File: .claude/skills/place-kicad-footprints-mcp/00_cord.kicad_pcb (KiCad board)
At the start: 2 copper layers, 38.7 x 20 mm, 7 parts, among them J1 Conn_01x02, J2 Conn_01x02, J3 Conn_01x02, U1 TPS62204DBV

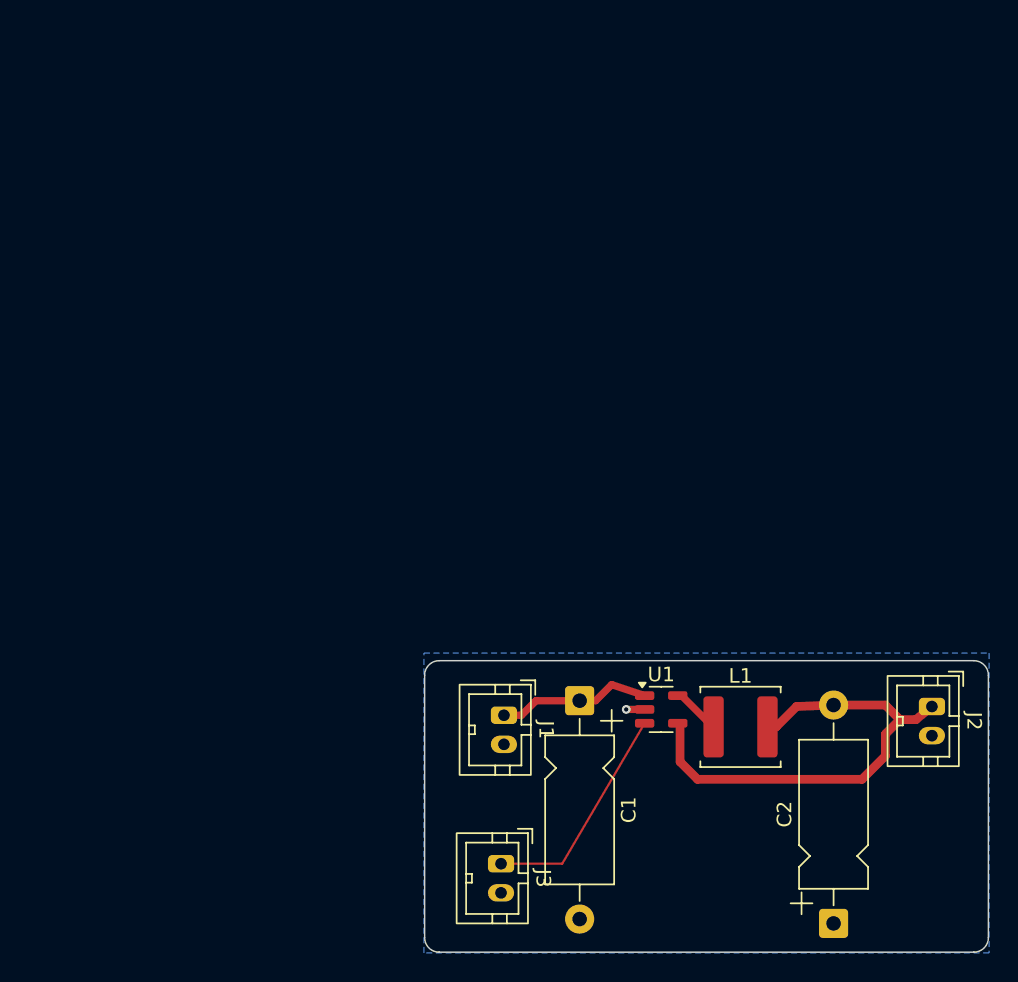
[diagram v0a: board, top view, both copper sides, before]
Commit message: 优化布线直角问题
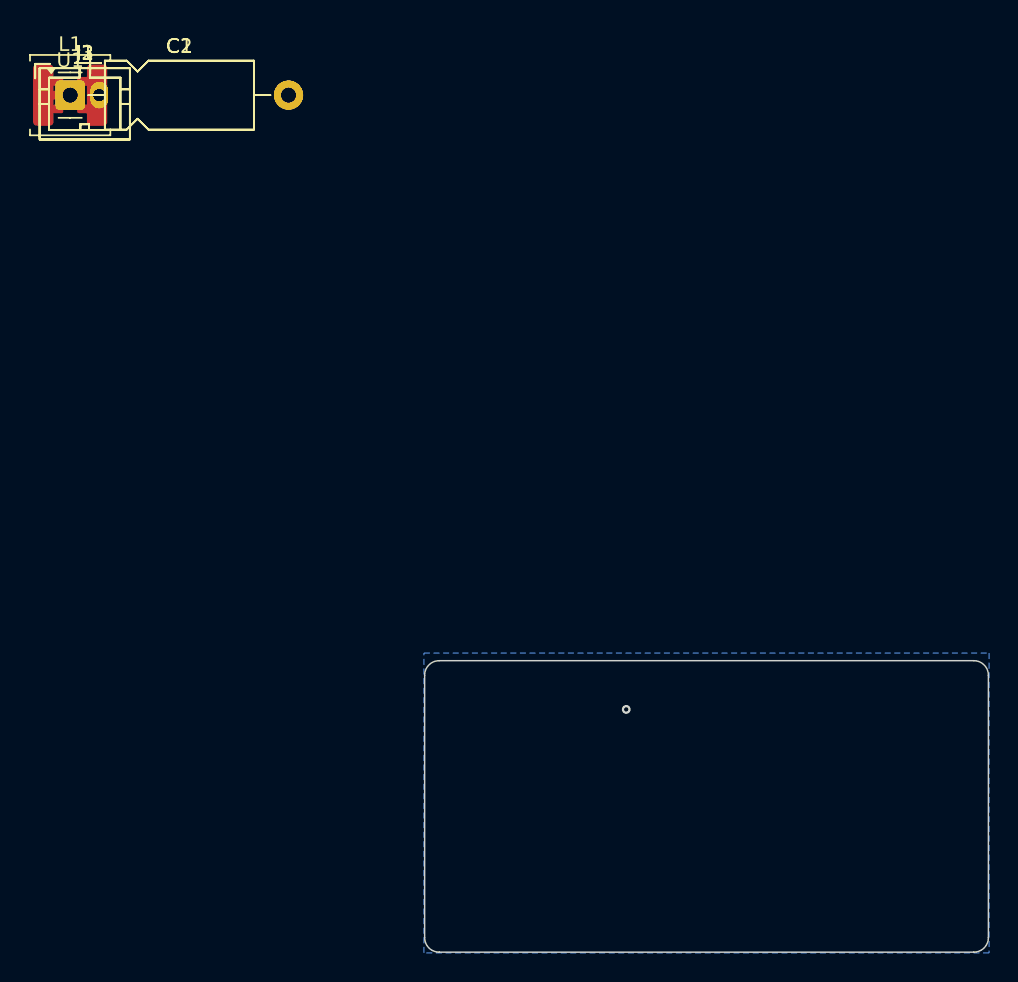
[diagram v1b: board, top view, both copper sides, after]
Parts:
- moved C2 77.4 mm to (0.00, 0.00), turned to 0 degrees
- moved J2 72.6 mm to (0.00, 0.00), turned to 0 degrees
- moved L1 63.3 mm to (0.00, 0.00)
- moved J3 60.5 mm to (0.00, 0.00), turned to 0 degrees
- moved U1 58.6 mm to (0.00, 0.00)
- moved C1 54.4 mm to (0.00, 0.00), turned to 0 degrees
- moved J1 52.0 mm to (0.00, 0.00), turned to 0 degrees
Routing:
- net /VOUT: track 33.5 -> 0.00 mm
- net /EN: track 15.4 -> 0.00 mm
- net /VIN: track 10.7 -> 0.00 mm
- net Net-(U1-SW): track 3.35 -> 0.00 mm
- net GND: track 1.26 -> 0.00 mm
